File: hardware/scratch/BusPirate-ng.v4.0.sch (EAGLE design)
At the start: 127 parts, among them CON1 CON-USB-F-MICRO-B, IC10 74LVC1G07DBV, IC11 IC_BUFF_SN74LVC1T45DBV, IC12 74LVC1G07DBV, IC13 IC_BUFF_SN74LVC1T45DBV, IC14 74LVC1G07DBV, IC15 IC_BUFF_SN74LVC1T45DBV, IC16 74LVC1G07DBV, IC17 IC_BUFF_SN74LVC1T45DBV, IC2 IC_MEM_23LC1024, IC3 IC_MEM_23LC1024, IC4 IC_74AC573, IC5 IC_BL1551, IC6 IC_BL1551, IC7 74HCT4066PW, IC8 74LVC1G07DBV, IC9 IC_BUFF_SN74LVC1T45DBV, J1 CON_HEADER_1X04, J2 CON_HEADER_1X03-PTH, J3 CON_HEADER_2X02-PTH, J5 CON_HEADER_1X10-RIGHT_ANGLED_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, U1 IC_FPGA_ICE40HX4K, U2 IC_UC_STM32F103ZX, U3 IC_MEM_AT45DB041D

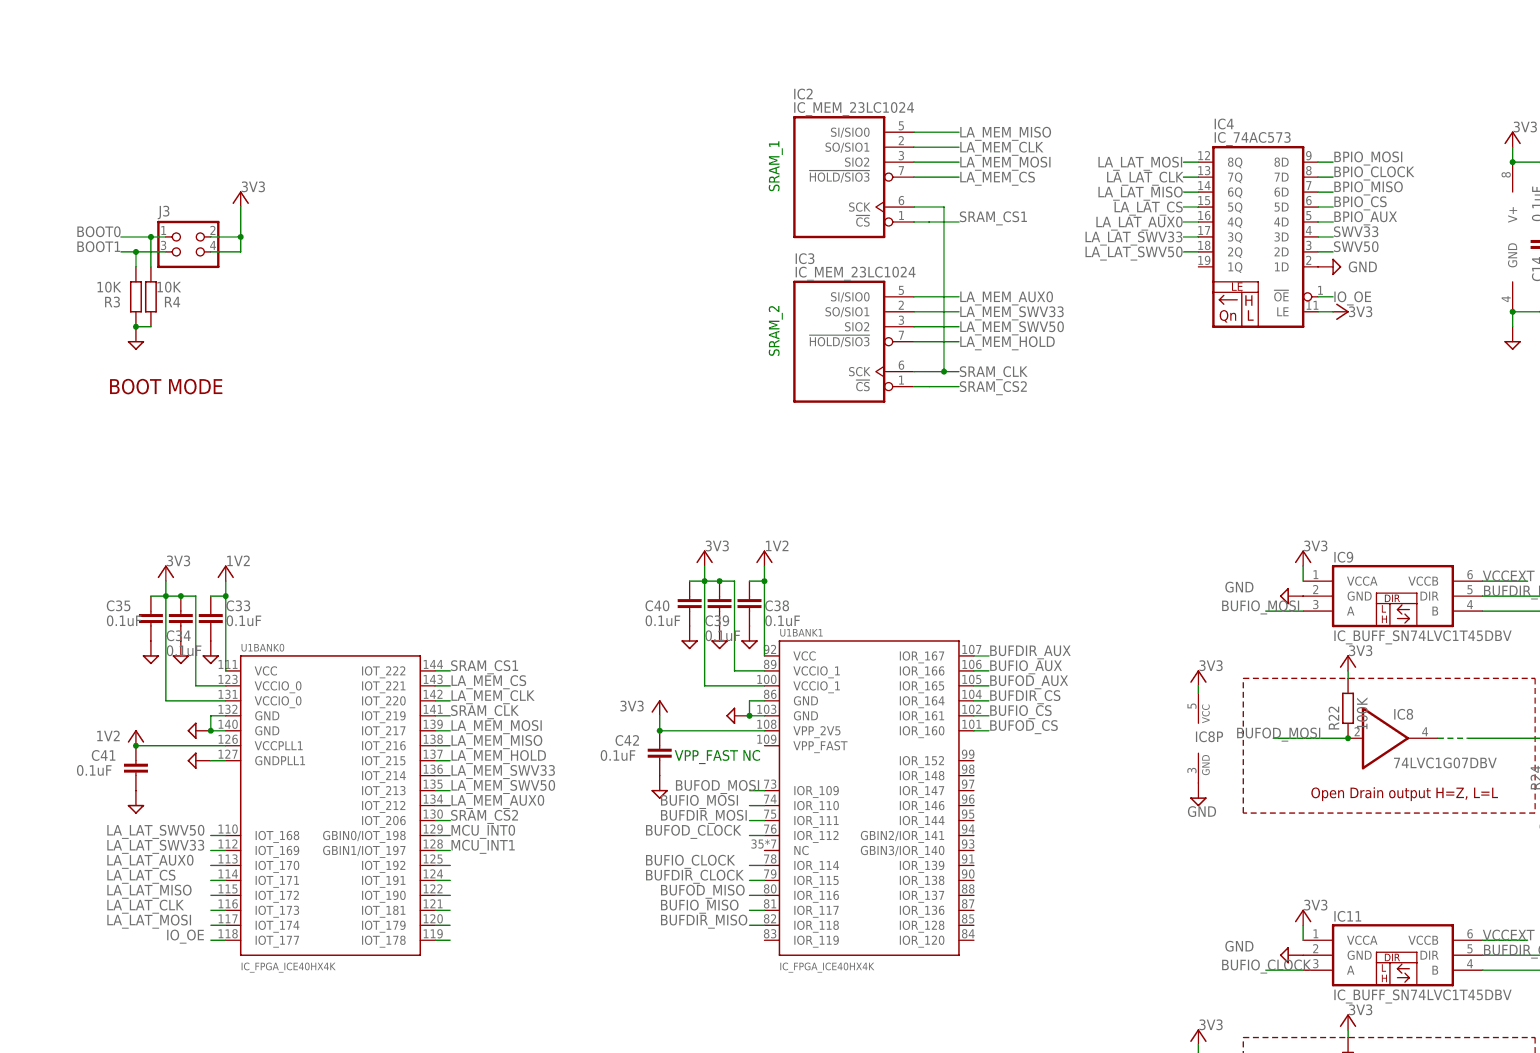
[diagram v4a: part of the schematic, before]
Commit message: moved LA_LAT_SWV50 from IOT_168 (bank-0) to IOR_152 LA_LAT_SWV33 from IOT_169 to IOR_148 LA_LAT_AUX0 from IOT_170 to IOR_147 LA_LAT_CS from IOT_171 to IOR_146 LA_LAT_MISO from IOT_172 to IOR_144 LA_LAT_CLK from IOT_173 to IOR_141 LA_LAT_MOSI from IOT_174 to IOR_140 IO_OE from IOT_177 to IOR_139 rearrange latch's connection
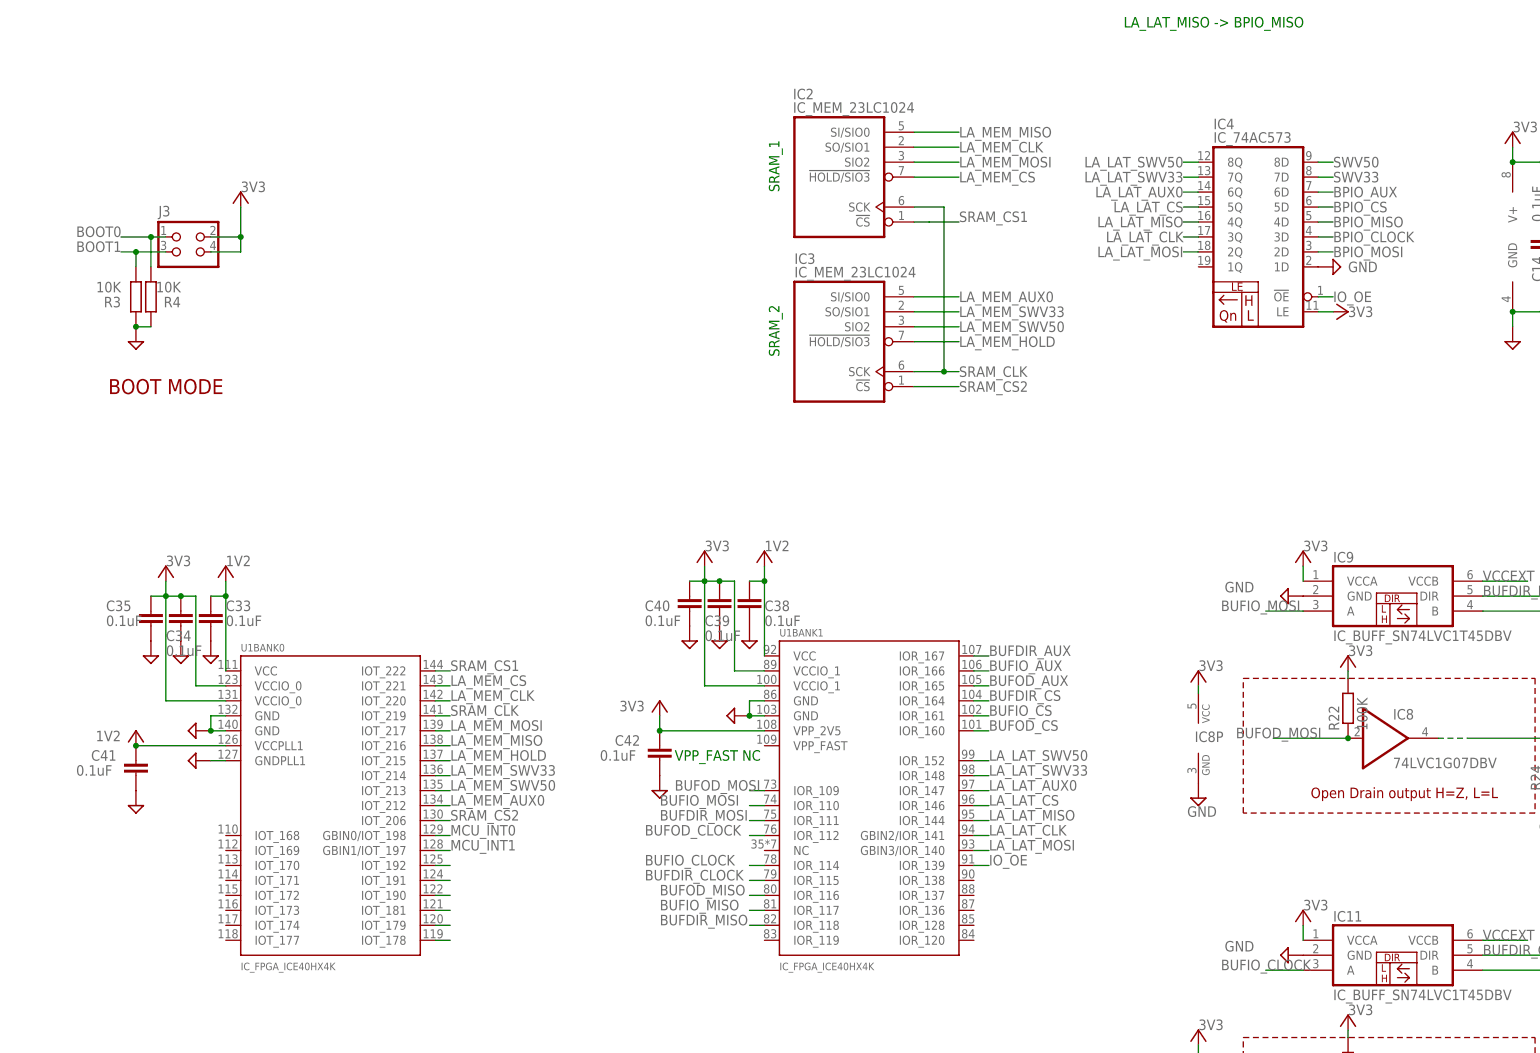
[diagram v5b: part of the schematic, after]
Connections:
- net BPIO_AUX: now also IC4IC.6D; no longer IC4IC.4D
- net BPIO_CLOCK: now also IC4IC.3D; no longer IC4IC.7D
- net BPIO_MISO: now also IC4IC.4D; no longer IC4IC.6D
- net BPIO_MOSI: now also IC4IC.2D; no longer IC4IC.8D
- net IO_OE: now also U1BANK1.IOR_139; no longer U1BANK0.IOT_177
- net LA_LAT_AUX0: now also IC4IC.6Q, U1BANK1.IOR_147; no longer IC4IC.4Q, U1BANK0.IOT_170
- net LA_LAT_CLK: now also IC4IC.3Q, U1BANK1.GBIN2/IOR_141; no longer IC4IC.7Q, U1BANK0.IOT_173
- net LA_LAT_CS: now also U1BANK1.IOR_146; no longer U1BANK0.IOT_171
- net LA_LAT_MISO: now also IC4IC.4Q, U1BANK1.IOR_144; no longer IC4IC.6Q, U1BANK0.IOT_172
- net LA_LAT_MOSI: now also IC4IC.2Q, U1BANK1.GBIN3/IOR_140; no longer IC4IC.8Q, U1BANK0.IOT_174
- net LA_LAT_SWV33: now also IC4IC.7Q, U1BANK1.IOR_148; no longer IC4IC.3Q, U1BANK0.IOT_169
- net LA_LAT_SWV50: now also IC4IC.8Q, U1BANK1.IOR_152; no longer IC4IC.2Q, U1BANK0.IOT_168
- net SWV33: now also IC4IC.7D; no longer IC4IC.3D
- net SWV50: now also IC4IC.8D; no longer IC4IC.2D
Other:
- note added: "LA_LAT_MISO -> BPIO_MISO"
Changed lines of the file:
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@@
 <text x="55.88" y="563.88" size="1.778" layer="91" rot="R90">SRAM_1</text>
 <text x="55.88" y="535.94" size="1.778" layer="91" rot="R90">SRAM_2</text>
+<text x="114.3" y="591.82" size="1.778" layer="91">LA_LAT_MISO -&gt; BPIO_MISO</text>
 </plain>
 <instances>
@@
 </segment>
 <segment>
-<pinref part="IC4" gate="IC" pin="3D"/>
-<wire x1="147.32" y1="556.26" x2="149.86" y2="556.26" width="0.1524" layer="91"/>
-<label x="149.86" y="556.26" size="1.778" layer="95"/>
-</segment>
-<segment>
 <pinref part="IC5" gate="IC" pin="A2"/>
 <wire x1="177.8" y1="139.7" x2="175.26" y2="139.7" width="0.1524" layer="91"/>
@@
 <label x="228.6" y="297.18" size="1.778" layer="95"/>
 </segment>
+<segment>
+<wire x1="147.32" y1="566.42" x2="149.86" y2="566.42" width="0.1524" layer="91"/>
+<pinref part="IC4" gate="IC" pin="7D"/>
+<label x="149.86" y="566.42" size="1.778" layer="95" align="center-left"/>
+</segment>
 </net>
 <net name="SWV50" class="0">
@@
 </segment>
 <segment>
-<pinref part="IC4" gate="IC" pin="2D"/>
-<wire x1="147.32" y1="553.72" x2="149.86" y2="553.72" width="0.1524" layer="91"/>
-<label x="149.86" y="553.72" size="1.778" layer="95"/>
-</segment>
-<segment>
 <pinref part="IC5" gate="IC" pin="A1"/>
 <wire x1="177.8" y1="147.32" x2="177.8" y2="175.26" width="0.1524" layer="91"/>
@@
 <label x="228.6" y="294.64" size="1.778" layer="95"/>
 </segment>
+<segment>
+<pinref part="IC4" gate="IC" pin="8D"/>
+<wire x1="147.32" y1="568.96" x2="149.86" y2="568.96" width="0.1524" layer="91"/>
+<label x="149.86" y="568.96" size="1.778" layer="95" align="center-left"/>
+</segment>
 </net>
 <net name="ADC2" class="0">
@@
 </segment>
 <segment>
-<pinref part="U1" gate="BANK0" pin="IOT_177"/>
-<wire x1="-38.1" y1="436.88" x2="-40.64" y2="436.88" width="0.1524" layer="91"/>
-<label x="-48.26" y="436.88" size="1.778" layer="95"/>
+<pinref part="U1" gate="BANK1" pin="IOR_139"/>
+<wire x1="88.9" y1="449.58" x2="91.44" y2="449.58" width="0.1524" layer="91"/>
+<label x="91.44" y="449.58" size="1.778" layer="95"/>
 </segment>
 </net>
@@
 </segment>
 <segment>
-<wire x1="147.32" y1="568.96" x2="149.86" y2="568.96" width="0.1524" layer="91"/>
-<pinref part="IC4" gate="IC" pin="8D"/>
-<label x="149.86" y="568.96" size="1.778" layer="95"/>
+<pinref part="IC4" gate="IC" pin="2D"/>
+<wire x1="147.32" y1="553.72" x2="149.86" y2="553.72" width="0.1524" layer="91"/>
+<label x="149.86" y="553.72" size="1.778" layer="95" align="center-left"/>
 </segment>
 </net>
@@
 </segment>
 <segment>
-<wire x1="147.32" y1="566.42" x2="149.86" y2="566.42" width="0.1524" layer="91"/>
-<pinref part="IC4" gate="IC" pin="7D"/>
-<label x="149.86" y="566.42" size="1.778" layer="95"/>
+<pinref part="IC4" gate="IC" pin="3D"/>
+<wire x1="147.32" y1="556.26" x2="149.86" y2="556.26" width="0.1524" layer="91"/>
+<label x="149.86" y="556.26" size="1.778" layer="95" align="center-left"/>
 </segment>
 </net>
@@
 </segment>
 <segment>
-<wire x1="147.32" y1="563.88" x2="149.86" y2="563.88" width="0.1524" layer="91"/>
-<pinref part="IC4" gate="IC" pin="6D"/>
-<label x="149.86" y="563.88" size="1.778" layer="95"/>
+<pinref part="IC4" gate="IC" pin="4D"/>
+<wire x1="147.32" y1="558.8" x2="149.86" y2="558.8" width="0.1524" layer="91"/>
+<label x="149.86" y="558.8" size="1.778" layer="95" align="center-left"/>
 </segment>
 </net>
@@
 <wire x1="147.32" y1="561.34" x2="149.86" y2="561.34" width="0.1524" layer="91"/>
 <pinref part="IC4" gate="IC" pin="5D"/>
-<label x="149.86" y="561.34" size="1.778" layer="95"/>
+<label x="149.86" y="561.34" size="1.778" layer="95" align="center-left"/>
 </segment>
 </net>
@@
 </segment>
 <segment>
-<pinref part="IC4" gate="IC" pin="4D"/>
-<wire x1="147.32" y1="558.8" x2="149.86" y2="558.8" width="0.1524" layer="91"/>
-<label x="149.86" y="558.8" size="1.778" layer="95"/>
+<wire x1="147.32" y1="563.88" x2="149.86" y2="563.88" width="0.1524" layer="91"/>
+<pinref part="IC4" gate="IC" pin="6D"/>
+<label x="149.86" y="563.88" size="1.778" layer="95" align="center-left"/>
 </segment>
 </net>
@@
 <net name="LA_LAT_MOSI" class="0">
 <segment>
-<wire x1="127" y1="568.96" x2="124.46" y2="568.96" width="0.1524" layer="91"/>
-<pinref part="IC4" gate="IC" pin="8Q"/>
-<label x="124.46" y="568.96" size="1.778" layer="95" align="center-right"/>
+<pinref part="IC4" gate="IC" pin="2Q"/>
+<wire x1="127" y1="553.72" x2="124.46" y2="553.72" width="0.1524" layer="91"/>
+<label x="124.46" y="553.72" size="1.778" layer="95" align="center-right"/>
 </segment>
 <segment>
-<pinref part="U1" gate="BANK0" pin="IOT_174"/>
-<wire x1="-38.1" y1="439.42" x2="-40.64" y2="439.42" width="0.1524" layer="91"/>
-<label x="-58.42" y="439.42" size="1.778" layer="95"/>
+<pinref part="U1" gate="BANK1" pin="GBIN3/IOR_140"/>
+<wire x1="88.9" y1="452.12" x2="91.44" y2="452.12" width="0.1524" layer="91"/>
+<label x="91.44" y="452.12" size="1.778" layer="95"/>
 </segment>
 </net>
@@
 <net name="LA_LAT_CLK" class="0">
 <segment>
-<wire x1="127" y1="566.42" x2="124.46" y2="566.42" width="0.1524" layer="91"/>
-<pinref part="IC4" gate="IC" pin="7Q"/>
-<label x="124.46" y="566.42" size="1.778" layer="95" align="center-right"/>
+<pinref part="IC4" gate="IC" pin="3Q"/>
+<wire x1="127" y1="556.26" x2="124.46" y2="556.26" width="0.1524" layer="91"/>
+<label x="124.46" y="556.26" size="1.778" layer="95" align="center-right"/>
 </segment>
 <segment>
-<pinref part="U1" gate="BANK0" pin="IOT_173"/>
-<wire x1="-38.1" y1="441.96" x2="-40.64" y2="441.96" width="0.1524" layer="91"/>
-<label x="-58.42" y="441.96" size="1.778" layer="95"/>
+<pinref part="U1" gate="BANK1" pin="GBIN2/IOR_141"/>
+<wire x1="88.9" y1="454.66" x2="91.44" y2="454.66" width="0.1524" layer="91"/>
+<label x="91.44" y="454.66" size="1.778" layer="95"/>
 </segment>
 </net>
 <net name="LA_LAT_MISO" class="0">
 <segment>
-<wire x1="127" y1="563.88" x2="124.46" y2="563.88" width="0.1524" layer="91"/>
-<pinref part="IC4" gate="IC" pin="6Q"/>
-<label x="124.46" y="563.88" size="1.778" layer="95" align="center-right"/>
+<pinref part="IC4" gate="IC" pin="4Q"/>
+<wire x1="127" y1="558.8" x2="124.46" y2="558.8" width="0.1524" layer="91"/>
+<label x="124.46" y="558.8" size="1.778" layer="95" align="center-right"/>
 </segment>
 <segment>
-<pinref part="U1" gate="BANK0" pin="IOT_172"/>
-<wire x1="-38.1" y1="444.5" x2="-40.64" y2="444.5" width="0.1524" layer="91"/>
-<label x="-58.42" y="444.5" size="1.778" layer="95"/>
+<pinref part="U1" gate="BANK1" pin="IOR_144"/>
+<wire x1="88.9" y1="457.2" x2="91.44" y2="457.2" width="0.1524" layer="91"/>
+<label x="91.44" y="457.2" size="1.778" layer="95"/>
 </segment>
 </net>
@@
 </segment>
 <segment>
-<pinref part="U1" gate="BANK0" pin="IOT_171"/>
-<wire x1="-38.1" y1="447.04" x2="-40.64" y2="447.04" width="0.1524" layer="91"/>
-<label x="-58.42" y="447.04" size="1.778" layer="95"/>
+<pinref part="U1" gate="BANK1" pin="IOR_146"/>
+<wire x1="88.9" y1="459.74" x2="91.44" y2="459.74" width="0.1524" layer="91"/>
+<label x="91.44" y="459.74" size="1.778" layer="95"/>
 </segment>
 </net>
 <net name="LA_LAT_AUX0" class="0">
 <segment>
-<pinref part="IC4" gate="IC" pin="4Q"/>
-<wire x1="127" y1="558.8" x2="124.46" y2="558.8" width="0.1524" layer="91"/>
-<label x="124.46" y="558.8" size="1.778" layer="95" align="center-right"/>
+<wire x1="127" y1="563.88" x2="124.46" y2="563.88" width="0.1524" layer="91"/>
+<pinref part="IC4" gate="IC" pin="6Q"/>
+<label x="124.46" y="563.88" size="1.778" layer="95" align="center-right"/>
 </segment>
 <segment>
-<pinref part="U1" gate="BANK0" pin="IOT_170"/>
-<wire x1="-38.1" y1="449.58" x2="-40.64" y2="449.58" width="0.1524" layer="91"/>
-<label x="-58.42" y="449.58" size="1.778" layer="95"/>
+<pinref part="U1" gate="BANK1" pin="IOR_147"/>
+<wire x1="88.9" y1="462.28" x2="91.44" y2="462.28" width="0.1524" layer="91"/>
+<label x="91.44" y="462.28" size="1.778" layer="95"/>
 </segment>
 </net>
 <net name="LA_LAT_SWV33" class="0">
 <segment>
-<pinref part="IC4" gate="IC" pin="3Q"/>
-<wire x1="127" y1="556.26" x2="124.46" y2="556.26" width="0.1524" layer="91"/>
-<label x="124.46" y="556.26" size="1.778" layer="95" align="center-right"/>
+<pinref part="U1" gate="BANK1" pin="IOR_148"/>
+<wire x1="88.9" y1="464.82" x2="91.44" y2="464.82" width="0.1524" layer="91"/>
+<label x="91.44" y="464.82" size="1.778" layer="95"/>
 </segment>
 <segment>
-<pinref part="U1" gate="BANK0" pin="IOT_169"/>
-<wire x1="-38.1" y1="452.12" x2="-40.64" y2="452.12" width="0.1524" layer="91"/>
-<label x="-58.42" y="452.12" size="1.778" layer="95"/>
+<wire x1="127" y1="566.42" x2="124.46" y2="566.42" width="0.1524" layer="91"/>
+<pinref part="IC4" gate="IC" pin="7Q"/>
+<label x="124.46" y="566.42" size="1.778" layer="95" align="center-right"/>
 </segment>
 </net>
 <net name="LA_LAT_SWV50" class="0">
 <segment>
-<pinref part="IC4" gate="IC" pin="2Q"/>
-<wire x1="127" y1="553.72" x2="124.46" y2="553.72" width="0.1524" layer="91"/>
-<label x="124.46" y="553.72" size="1.778" layer="95" align="center-right"/>
+<pinref part="U1" gate="BANK1" pin="IOR_152"/>
+<wire x1="88.9" y1="467.36" x2="91.44" y2="467.36" width="0.1524" layer="91"/>
+<label x="91.44" y="467.36" size="1.778" layer="95"/>
 </segment>
 <segment>
-<pinref part="U1" gate="BANK0" pin="IOT_168"/>
-<wire x1="-38.1" y1="454.66" x2="-40.64" y2="454.66" width="0.1524" layer="91"/>
-<label x="-58.42" y="454.66" size="1.778" layer="95"/>
+<pinref part="IC4" gate="IC" pin="8Q"/>
+<wire x1="127" y1="568.96" x2="124.46" y2="568.96" width="0.1524" layer="91"/>
+<label x="124.46" y="568.96" size="1.778" layer="95" align="center-right"/>
 </segment>
 </net>

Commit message: convert switched 5V and 3.3V voltage divider resistors R9, R10, R11, R12 to resistor array moved ADC4 from PC4 (ADC12_IN14) to PA4 (ADC12_IN4) ADC3 from PC5 (ADC12_IN15) to PA5 (ADC12_IN5) ADC2 from PC3 (ADC123_IN13) to PA7 (ADC12_IN7) ADC6 from PA7 (ADC12_IN7) to PC4 (ADC12_IN14) joined VEXTPU pull-down resistor R21 to resistor network RN3 move MCU V50PU control pin from PG0 to PF15 move MCU V33PU control pin from PG1 to PG0 move MCU VEXTPU control pin from PF15 to PG1 swapped MCU pin V50PU and VEXTPU PF15 and PG1
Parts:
- removed R10, R11, R12, R9: 10K, resistor:R-EU_R0603
- removed R21: 10k, dp_devices:RESISTOR-0603
- added RN2: 10k, dp_devices:RNETWORK
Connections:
- removed net N$34: U2U.PA5/SPI1_SCK('0')/ADC12_IN5
- new net N$23: U2U.ADC123_IN12/PC2
- new net N$25: U2U.ADC12_IN15/PC5
- net ADC2: now also U2U.PA7/SPI1_MOSI('0')/TIM8_CH1N/ADC12_IN7/TIM3_CH2('00')/TIM1_CH1N('01'); no longer U2U.ADC123_IN13/PC3
- net ADC3: now also RN2C.2, RN2D.2, U2U.PA5/SPI1_SCK('0')/ADC12_IN5; no longer R10.2, R9.2, U2U.ADC12_IN15/PC5
- net ADC4: now also RN2A.2, RN2B.2, U2U.PA4/SPI1_NSS('0')/USART2_CK('0')/ADC12_IN4; no longer R11.2, R12.2, U2U.ADC12_IN14/PC4
- net ADC6: now also U2U.ADC12_IN14/PC4; no longer U2U.PA7/SPI1_MOSI('0')/TIM8_CH1N/ADC12_IN7/TIM3_CH2('00')/TIM1_CH1N('01')
- net GND: now also RN1A.1, RN2A.1, RN2D.1, RN3C.1; no longer R10.1, R12.1, R21.2, RN1B.1
- net SWV33: now also RN2C.1; no longer R9.1
- net SWV50: now also RN2B.1; no longer R11.1
- net V33PU: now also U2U.PG0/FT/FSMC_A10; no longer U2U.PG1/FT/FSMC_A11
- net V50PU: now also RN3C.2, U2U.PG1/FT/FSMC_A11; no longer RN3A.2, U2U.PG0/FT/FSMC_A10
- net VEXTERN: now also RN1B.1; no longer RN1A.1
- net VEXTPU: now also RN3A.2; no longer R21.1
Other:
- moved on the sheet: R13, R14, R7, R8, RN1A, RN1B, RN1C, RN1D, RN3A

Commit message: added 0.1uF decoupling caps on both power pins of 74LVC buffer chips move latch's IO_OE from FPGA's IOR_139 pin to IOR_138 move LA_MEM_AUX0 from IOT_212 to IOT_169 move LA_MEM_SWV50 from IOT_213 to IOT_170 move LA_MEM_SWV33 from IOT_214 to IOT_171 move LA_MEM_HOLD from IOT_215 to IOT_172 move SRAM_CS2 from IOT_206 to IOT_173
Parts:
- added C1, C10, C2, C3, C4, C5, C6, C7, C8, C9: 0.1uF, rcl:C-EUC0603
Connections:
- new net LA_LAT_AUX1: IC4IC.1Q, U1BANK1.IOR_139
- new net N$24: U1BANK0.IOT_168
- new net N$48: U1BANK0.IOT_174
- new net N$49: U1BANK0.IOT_177
- net 3V3: now also C1.1, C3.1, C5.1, C7.1, C9.1
- net GND: now also C1.2, C10.1, C2.1, C3.2, C4.1, C5.2, C6.1, C7.2, C8.1, C9.2
- net IO_OE: now also U1BANK1.IOR_138; no longer U1BANK1.IOR_139
- net LA_MEM_AUX0: now also U1BANK0.IOT_169; no longer U1BANK0.IOT_212
- net LA_MEM_HOLD: now also U1BANK0.IOT_172; no longer U1BANK0.IOT_215
- net LA_MEM_SWV33: now also U1BANK0.IOT_171; no longer U1BANK0.IOT_214
- net LA_MEM_SWV50: now also U1BANK0.IOT_170; no longer U1BANK0.IOT_213
- net SRAM_CS2: now also U1BANK0.IOT_173; no longer U1BANK0.IOT_206
- net VCCEXT: now also C10.2, C2.2, C4.2, C6.2, C8.2
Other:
- moved on the sheet: IC14, IC14P, IC15, R23, R26, R29, R31, R32, R33, R35

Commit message: Renamed nets name and wire missing connection -renamed SRAM nets -renamed LATCH nets -wired FSMC control pins. FSMC_NOE_OE, FSMC_NWE_WE and FSMC_NE3_CE to FPGA 11, 12 and 22. -wired PWM pin PC6 (TIM8_CH1/TIM3_CH1) to FPGA 21/GBIN6
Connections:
- net IO_OE renamed LAT_OE
- net LA_LAT_AUX0 renamed LAT_AUX0
- net LA_LAT_AUX1 renamed LAT_AUX1
- net LA_LAT_CLK renamed LAT_CLK
- net LA_LAT_CS renamed LAT_CS
- net LA_LAT_MISO renamed LAT_MISO
- net LA_LAT_MOSI renamed LAT_MOSI
- net LA_LAT_SWV33 renamed LAT_SWV33
- net LA_LAT_SWV50 renamed LAT_SWV50
- net LA_MEM_AUX0 renamed SRAM1_SIO0
- net LA_MEM_CLK renamed SRAM0_SIO1
- net LA_MEM_CS renamed SRAM0_SIO3
- net LA_MEM_HOLD renamed SRAM1_SIO3
- net LA_MEM_MISO renamed SRAM0_SIO0
- net LA_MEM_MOSI renamed SRAM0_SIO2
- net LA_MEM_SWV33 renamed SRAM1_SIO1
- net LA_MEM_SWV50 renamed SRAM1_SIO2
- net SRAM_CLK renamed SRAM_CLOCK
- net SRAM_CS1 renamed SRAM0_CS
- net SRAM_CS2 renamed SRAM1_CS
- removed net N$15: U1BANK3.IOL_8A
- removed net N$21: U1BANK3.GBIN6/IOL_14A
- new net N$34: U2U.PD13/FT/FSMC_A18/TIM4_CH2('1')
- new net N$43: U2U.PD12/FT/FSMC_A17/USART3_RTS('11')/TIM4_CH1('1')
- new net N$45: U2U.PA10/FT/USART1_RX('0')/TIM1_CH3('00'OR'01')
- new net N$46: U2U.PA9/FT/USART1_TX('0')/TIM1_CH2('00'OR'01')
- new net N$47: U2U.PA15/FT/JTDI/SPI3_NSS('0')/TIM2_CH1_ETR('11')/SPI1_NSS('1')
- new net N$50: U2U.PG3/FT/FSMC_A13
- new net N$51: U2U.PG4/FT/FSMC_A14
- new net N$52: U2U.PG5/FT/FSMC_A15
- new net N$53: U2U.PG8/FT
- new net N$54: U2U.PG9/FT/FSMC_NE2/FSMC_NCE3
- new net PWM: U1BANK3.GBIN6/IOL_14A, U2U.TIM8_CH1/TIM3_CH1('11')/FT/PC6
- net FSMC_NE3_CE: now also U1BANK3.IOL_14B
- net FSMC_NOE_OE: now also U1BANK3.IOL_8A
- net FSMC_NWE_WE: now also U1BANK3.IOL_8B
- net N$19: now also U2U.TIM8_CH2/TIM3_CH2('11')/FT/PC7; no longer U1BANK3.IOL_8B
- net N$22: now also U2U.TIM8_CH3/TIM3_CH3('11')/FT/PC8; no longer U1BANK3.IOL_14B
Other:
- moved on the sheet: C55
